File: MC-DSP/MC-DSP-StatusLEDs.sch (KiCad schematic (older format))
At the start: 6 parts

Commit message: ADC refs, FTDI changes, and more
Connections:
- net GlobalResetIndicator renamed SafeStateIndicator
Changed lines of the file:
@@
 $Descr A4 11693 8268
 encoding utf-8
-Sheet 7 9
+Sheet 6 9
 Title ""
 Date ""
@@
 	7000 4500 6800 4500
 Text HLabel 5500 3500 0    50   Input ~ 0
-GlobalResetIndicator
+SafeStateIndicator
 Text HLabel 5500 4000 0    50   Input ~ 0
 GPIOLED1

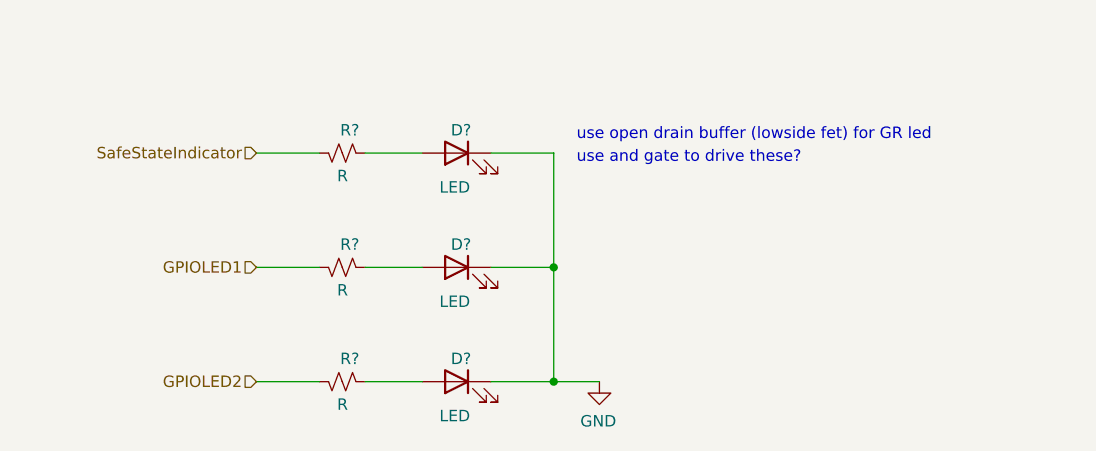
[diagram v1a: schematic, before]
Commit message: All parts labeled, just need to pick passives basically.
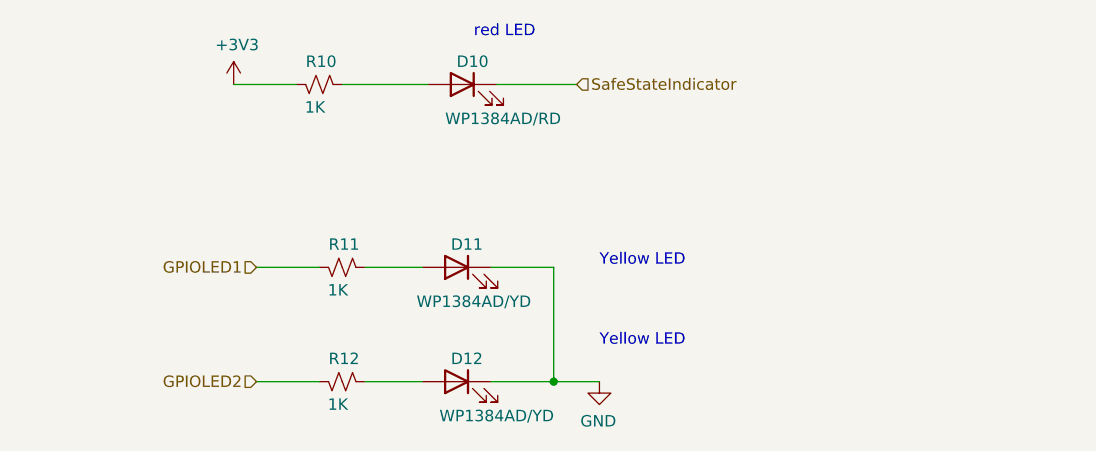
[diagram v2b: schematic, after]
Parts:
- removed D?: LED, symbol Device:LED
- added D12: WP1384AD/YD, LED_THT:LED_D3.0mm, symbol Device:LED
- D10: renamed from D?; value LED -> WP1384AD/RD; footprint (none) -> LED_THT:LED_D3.0mm
- D11: renamed from D?; value LED -> WP1384AD/YD; footprint (none) -> LED_THT:LED_D3.0mm
- R10, R11, R12: renamed from R?; value R -> 1K; footprint (none) -> Resistor_SMD:R_0603_1608Metric_Pad0.98x0.95mm_HandSolder
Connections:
- net GND: now also D12.1 (K); no longer D10.1 (K)
- net SafeStateIndicator: now also D10.1 (K); no longer R10.1
- net at R12.2: now also D12.2 (A)
- new net +3V3: R10.1
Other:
- note added: "Yellow LED"
- note added: "red LED"
- note removed: "use and gate to drive these?"
- note removed: "use open drain buffer (lowside fet) for GR led"
- moved on the sheet: D10, R10
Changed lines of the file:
@@
 $Descr A4 11693 8268
 encoding utf-8
-Sheet 6 9
+Sheet 5 9
 Title ""
 Date ""
@@
 $EndDescr
 $Comp
-L Device:R_Small_US R?
+L Device:R_Small_US R12
 U 1 1 61998842
 P 5875 4500
-F 0 "R?" V 5775 4425 50  0000 L CNN
-F 1 "R" V 5975 4475 50  0000 L CNN
-F 2 "" H 5875 4500 50  0001 C CNN
-F 3 "~" H 5875 4500 50  0001 C CNN
+F 0 "R12" V 5775 4425 50  0000 L CNN
+F 1 "1K" V 5975 4475 50  0000 L CNN
+F 2 "Resistor_SMD:R_0603_1608Metric_Pad0.98x0.95mm_HandSolder" H 5875 4500 50  0001 C CNN
+F 3 "?" H 5875 4500 50  0001 C CNN
 	1    5875 4500
 	0    -1   1    0
 $EndComp
-$Comp
-L Device:LED D?
-U 1 1 61998843
-P 6375 4500
-F 0 "D?" H 6400 4600 50  0000 R CNN
-F 1 "LED" H 6450 4350 50  0000 R CNN
-F 2 "" H 6375 4500 50  0001 C CNN
-F 3 "~" H 6375 4500 50  0001 C CNN
-	1    6375 4500
-	-1   0    0    -1
-$EndComp
-Wire Wire Line
-	5975 4500 6225 4500
-Wire Wire Line
-	6525 4500 6800 4500
 $Comp
 L power:GND #PWR?
@@
 	5500 4000 5775 4000
 Wire Wire Line
-	6525 3500 6800 3500
-Wire Wire Line
 	7000 4500 6800 4500
-Text HLabel 5500 3500 0    50   Input ~ 0
+Text HLabel 6900 3200 2    50   Input ~ 0
 SafeStateIndicator
 Text HLabel 5500 4000 0    50   Input ~ 0
@@
 Connection ~ 6800 4500
 Wire Wire Line
-	5500 3500 5775 3500
+	5400 3200 5675 3200
 Wire Wire Line
 	6525 4000 6800 4000
 $Comp
-L Device:R_Small_US R?
+L Device:R_Small_US R11
 U 1 1 61A0FC60
 P 5875 4000
-F 0 "R?" V 5775 3925 50  0000 L CNN
-F 1 "R" V 5975 3975 50  0000 L CNN
-F 2 "" H 5875 4000 50  0001 C CNN
-F 3 "~" H 5875 4000 50  0001 C CNN
+F 0 "R11" V 5775 3925 50  0000 L CNN
+F 1 "1K" V 5975 3975 50  0000 L CNN
+F 2 "Resistor_SMD:R_0603_1608Metric_Pad0.98x0.95mm_HandSolder" H 5875 4000 50  0001 C CNN
+F 3 "?" H 5875 4000 50  0001 C CNN
 	1    5875 4000
 	0    -1   1    0
 $EndComp
 $Comp
-L Device:LED D?
+L Device:LED D11
 U 1 1 61A0FC66
 P 6375 4000
-F 0 "D?" H 6400 4100 50  0000 R CNN
-F 1 "LED" H 6450 3850 50  0000 R CNN
-F 2 "" H 6375 4000 50  0001 C CNN
-F 3 "~" H 6375 4000 50  0001 C CNN
+F 0 "D11" H 6400 4100 50  0000 R CNN
+F 1 "WP1384AD/YD" H 6550 3850 50  0000 R CNN
+F 2 "LED_THT:LED_D3.0mm" H 6375 4000 50  0001 C CNN
+F 3 "https://www.digikey.com/en/products/detail/kingbright/WP1384AD-YD/3084082?s=N4IgjCBcoLQBxVAYygMwIYBsDOBTANCAPZQDaIA7AKwAsIAugL6OEBMZIA6gApgDMcGgEEAIgHoAmiIaMgA" H 6375 4000 50  0001 C CNN
 	1    6375 4000
 	-1   0    0    -1
@@
 	5975 4000 6225 4000
 $Comp
-L Device:R_Small_US R?
+L Device:R_Small_US R10
 U 1 1 61A116D4
-P 5875 3500
-F 0 "R?" V 5775 3425 50  0000 L CNN
-F 1 "R" V 5975 3475 50  0000 L CNN
-F 2 "" H 5875 3500 50  0001 C CNN
-F 3 "~" H 5875 3500 50  0001 C CNN
-	1    5875 3500
+P 5775 3200
+F 0 "R10" V 5675 3125 50  0000 L CNN
+F 1 "1K" V 5875 3175 50  0000 L CNN
+F 2 "Resistor_SMD:R_0603_1608Metric_Pad0.98x0.95mm_HandSolder" H 5775 3200 50  0001 C CNN
+F 3 "?" H 5775 3200 50  0001 C CNN
+	1    5775 3200
 	0    -1   1    0
 $EndComp
+Wire Wire Line
+	6800 4000 6800 4500
 $Comp
-L Device:LED D?
+L power:+3V3 #PWR?
+U 1 1 634D541A
+P 5400 3200
+F 0 "#PWR?" H 5400 3050 50  0001 C CNN
+F 1 "+3V3" H 5415 3373 50  0000 C CNN
+F 2 "" H 5400 3200 50  0001 C CNN
+F 3 "" H 5400 3200 50  0001 C CNN
+	1    5400 3200
+	1    0    0    -1
+$EndComp
+Wire Wire Line
+	5875 3200 6250 3200
+Wire Wire Line
+	6550 3200 6900 3200
+Text Notes 6450 3000 0    50   ~ 0
+red LED
+Text Notes 7000 4000 0    50   ~ 0
+Yellow LED
+Text Notes 7000 4350 0    50   ~ 0
+Yellow LED
+$Comp
+L Device:LED D10
 U 1 1 61A116DA
-P 6375 3500
-F 0 "D?" H 6400 3600 50  0000 R CNN
-F 1 "LED" H 6450 3350 50  0000 R CNN
-F 2 "" H 6375 3500 50  0001 C CNN
-F 3 "~" H 6375 3500 50  0001 C CNN
-	1    6375 3500
+P 6400 3200
+F 0 "D10" H 6425 3300 50  0000 R CNN
+F 1 "WP1384AD/RD" H 6475 3050 50  0000 R CNN
+F 2 "LED_THT:LED_D3.0mm" H 6400 3200 50  0001 C CNN
+F 3 "https://www.digikey.com/en/products/detail/kingbright/WP1384AD-ID/3084080?s=N4IgjCBcoLQBxVAYygMwIYBsDOBTANCAPZQDaIA7AKwAsIAugL6OEBMZIA6gApgDMcGgEEAIgHoAkiIaMgA" H 6400 3200 50  0001 C CNN
+	1    6400 3200
 	-1   0    0    -1
 $EndComp
 Wire Wire Line
-	5975 3500 6225 3500
+	5975 4500 6225 4500
 Wire Wire Line
-	6800 3500 6800 4000
-Connection ~ 6800 4000
-Wire Wire Line
-	6800 4000 6800 4500
-Text Notes 6900 3450 0    50   ~ 0
-use open drain buffer (lowside fet) for GR led
-Text Notes 6900 3550 0    50   ~ 0
-use and gate to drive these?
+	6525 4500 6800 4500
+$Comp
+L Device:LED D12
+U 1 1 62D580B6
+P 6375 4500
+F 0 "D12" H 6400 4600 50  0000 R CNN
+F 1 "WP1384AD/YD" H 6450 4350 50  0000 R CNN
+F 2 "LED_THT:LED_D3.0mm" H 6375 4500 50  0001 C CNN
+F 3 "https://www.digikey.com/en/products/detail/kingbright/WP1384AD-YD/3084082?s=N4IgjCBcoLQBxVAYygMwIYBsDOBTANCAPZQDaIA7AKwAsIAugL6OEBMZIA6gApgDMcGgEEAIgHoAmiIaMgA" H 6375 4500 50  0001 C CNN
+	1    6375 4500
+	-1   0    0    -1
+$EndComp
 $EndSCHEMATC
